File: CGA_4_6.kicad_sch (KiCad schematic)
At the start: 20 parts, among them U1 74S112, U15 74LS00, U16 74LS04, U2 74LS74, U20 74LS04, U22 74LS51, U23 74LS32, U25 74LS00, U26 74S04, U27 74LS51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

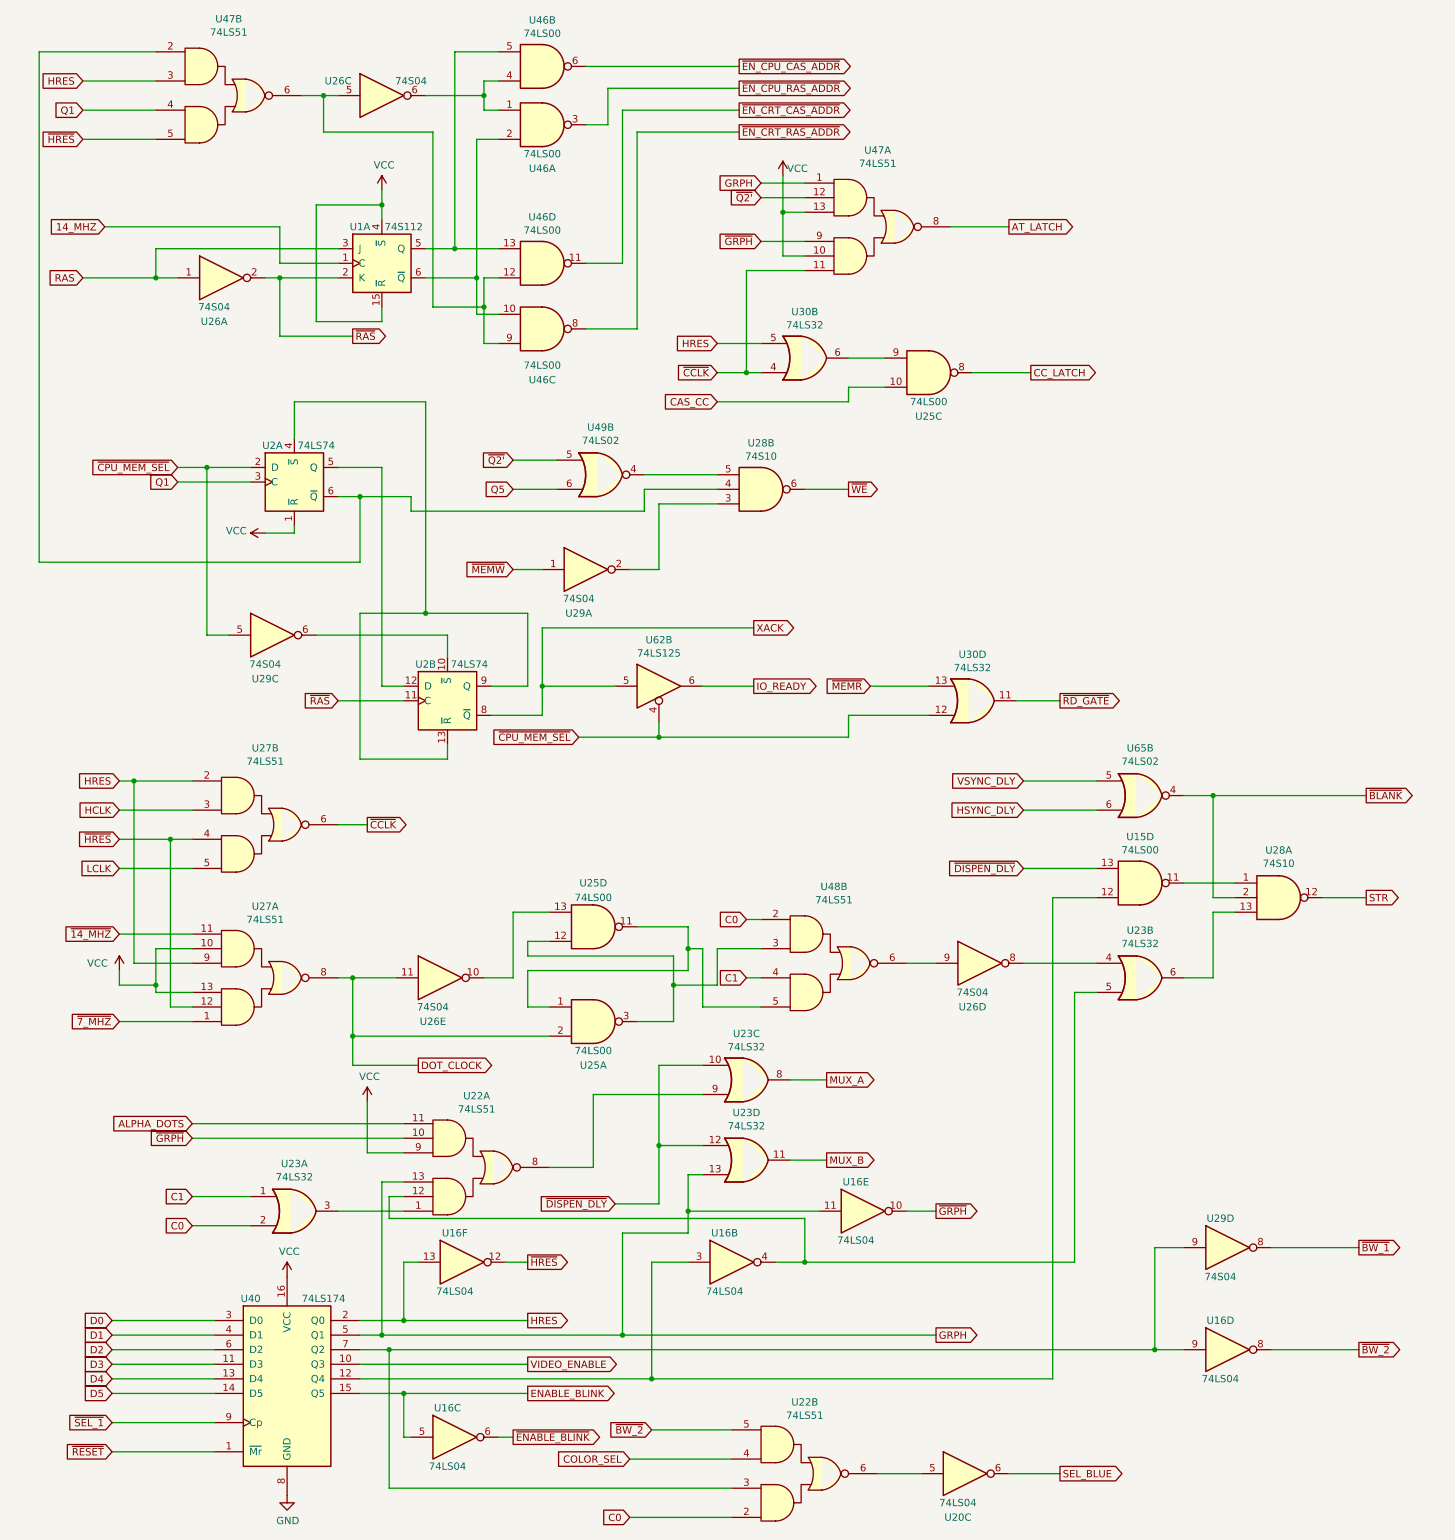
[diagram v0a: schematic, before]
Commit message: Fix Q1' naming thanks to Michael Karcher
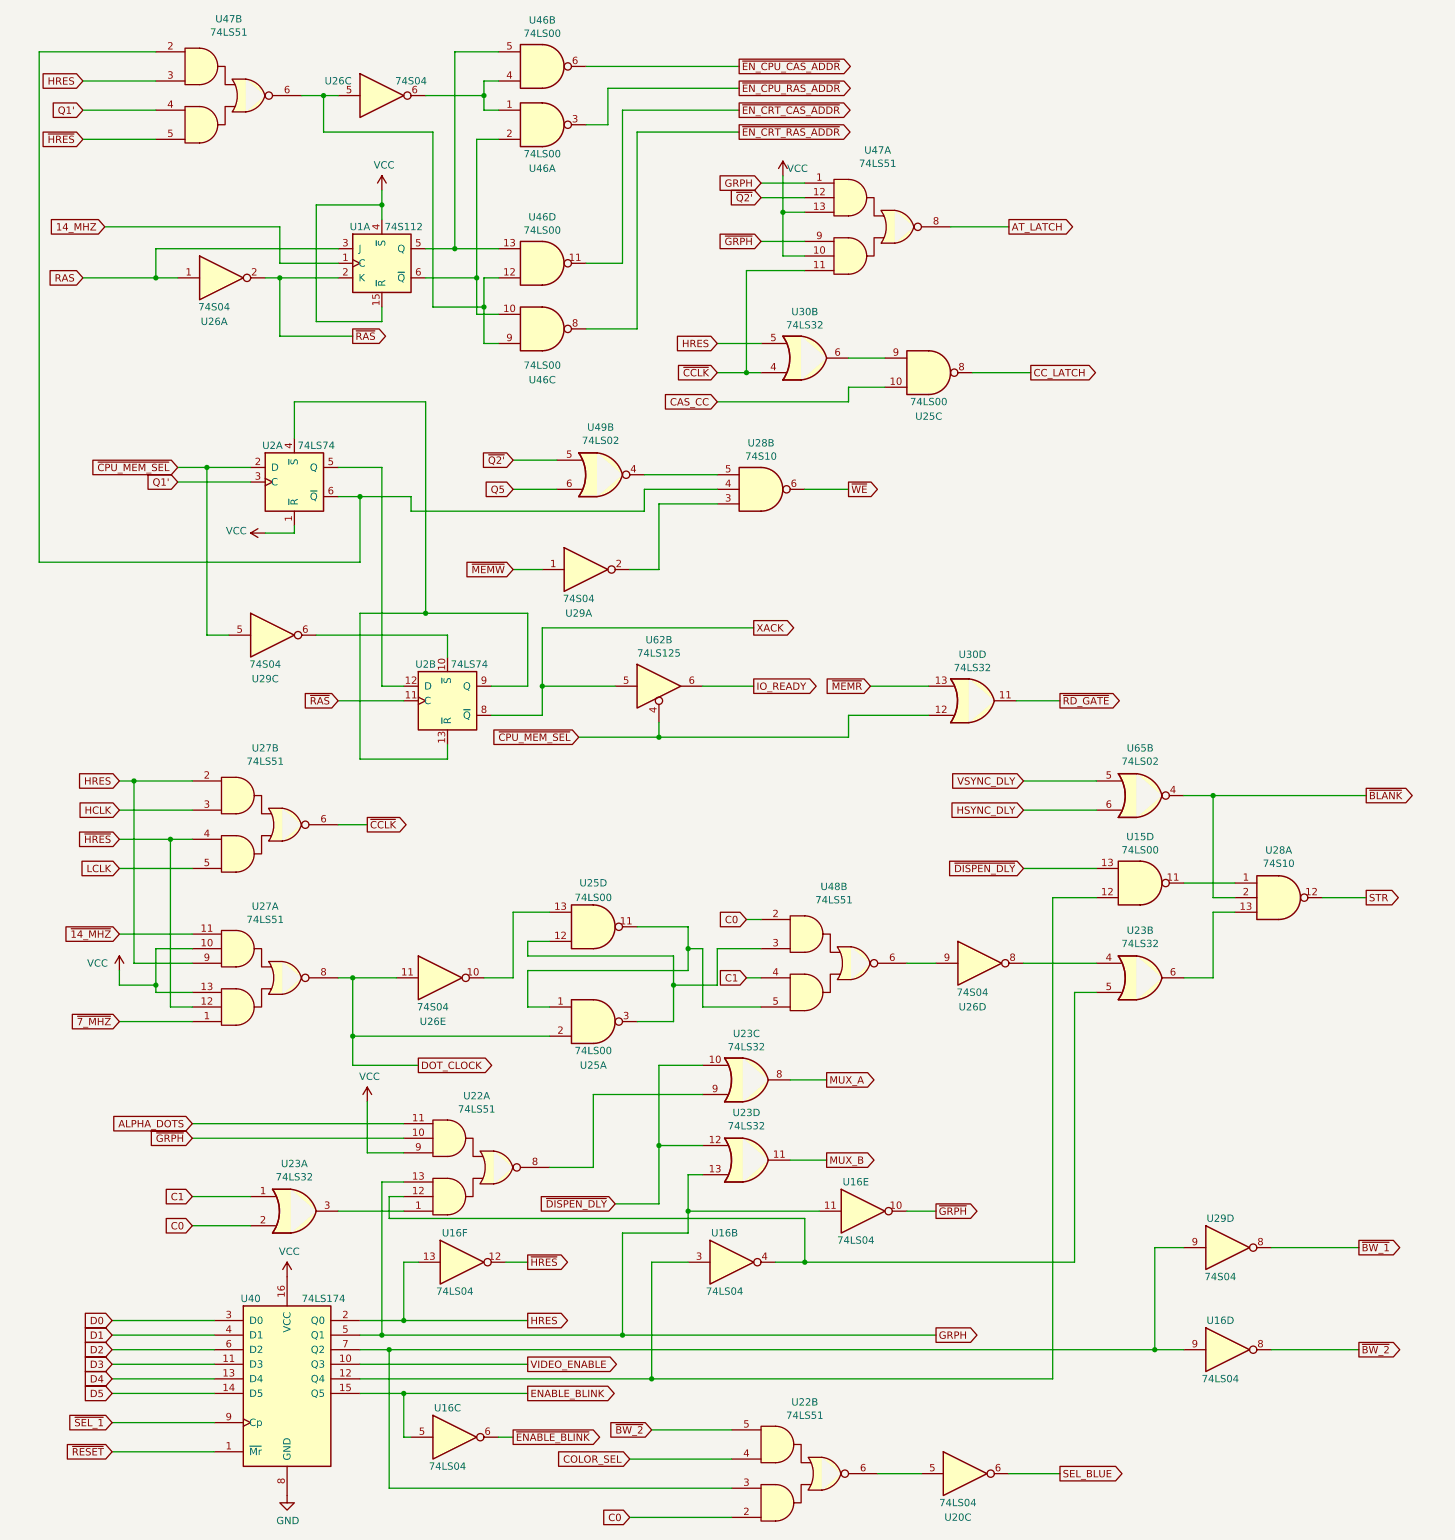
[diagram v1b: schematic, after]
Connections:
- net Q1 renamed Q1'
